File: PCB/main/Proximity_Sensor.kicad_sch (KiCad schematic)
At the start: 8 parts, among them U4 VL6180XV0NR_1

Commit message: Add sheet properties
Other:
- company: (none) -> University of Cape Town
- title: (none) -> Proximity Sensor
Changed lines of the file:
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@@
 (kicad_sch (version 20211123) (generator eeschema)
   (paper "A4")
+  (title_block
+    (title "Proximity Sensor")
+    (date "2022-03-09")
+    (rev "v1.0")
+    (company "University of Cape Town")
+    (comment 4 "Author: Kelvin Yankey")
+  )
   (junction (at 172.72 87.63) (diameter 0) (color 0 0 0 0)
   )

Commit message: Add changes
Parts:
- renumbered C5 to C7, C6 to C8, D2 to D8, D3 to D9, R7 to R11, R9 to R12, R12 to R13, U4 to U6
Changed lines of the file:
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@@
   (symbol (lib_id "Device:R") (at 85.09 46.99 0) (unit 1)
     (in_bom yes) (on_board yes) (fields_autoplaced)
-    (property "Reference" "R7" (id 0) (at 87.63 45.7199 0)
+    (property "Reference" "R11" (id 0) (at 87.63 45.7199 0)
       (effects (font (size 1.27 1.27)) (justify left))
     )
@@
   (symbol (lib_id "Device:C_Polarized") (at 151.13 53.34 270) (unit 1)
     (in_bom yes) (on_board yes) (fields_autoplaced)
-    (property "Reference" "C5" (id 0) (at 152.019 45.72 90))
+    (property "Reference" "C7" (id 0) (at 152.019 45.72 90))
     (property "Value" "100n" (id 1) (at 152.019 48.26 90))
     (property "Footprint" "Capacitor_SMD:C_01005_0402Metric" (id 2) (at 147.32 54.3052 0)
@@
   (symbol (lib_id "Device:R") (at 172.72 95.25 0) (unit 1)
     (in_bom yes) (on_board yes) (fields_autoplaced)
-    (property "Reference" "R12" (id 0) (at 175.26 93.9799 0)
+    (property "Reference" "R13" (id 0) (at 175.26 93.9799 0)
       (effects (font (size 1.27 1.27)) (justify left))
     )
@@
   (symbol (lib_id "Device:R") (at 85.09 55.88 0) (unit 1)
     (in_bom yes) (on_board yes) (fields_autoplaced)
-    (property "Reference" "R9" (id 0) (at 87.63 54.6099 0)
+    (property "Reference" "R12" (id 0) (at 87.63 54.6099 0)
       (effects (font (size 1.27 1.27)) (justify left))
     )
@@
   (symbol (lib_id "Device:C_Polarized") (at 151.13 67.31 270) (unit 1)
     (in_bom yes) (on_board yes) (fields_autoplaced)
-    (property "Reference" "C6" (id 0) (at 152.019 59.69 90))
+    (property "Reference" "C8" (id 0) (at 152.019 59.69 90))
     (property "Value" "4.7n" (id 1) (at 152.019 62.23 90))
     (property "Footprint" "" (id 2) (at 147.32 68.2752 0)
@@
   (symbol (lib_id "Diode:BZT52Bxx") (at 85.09 71.12 270) (unit 1)
     (in_bom yes) (on_board yes) (fields_autoplaced)
-    (property "Reference" "D2" (id 0) (at 87.63 69.8499 90)
+    (property "Reference" "D8" (id 0) (at 87.63 69.8499 90)
       (effects (font (size 1.27 1.27)) (justify left))
     )
@@
   (symbol (lib_id "Device:LED") (at 172.72 102.87 90) (unit 1)
     (in_bom yes) (on_board yes) (fields_autoplaced)
-    (property "Reference" "D3" (id 0) (at 176.53 103.1874 90)
+    (property "Reference" "D9" (id 0) (at 176.53 103.1874 90)
       (effects (font (size 1.27 1.27)) (justify right))
     )
@@
   (symbol (lib_id "EEE3088Components:VL6180XV0NR_1") (at 185.42 59.69 0) (unit 1)
     (in_bom yes) (on_board yes) (fields_autoplaced)
-    (property "Reference" "U4" (id 0) (at 210.82 52.07 0))
+    (property "Reference" "U6" (id 0) (at 210.82 52.07 0))
     (property "Value" "VL6180XV0NR_1" (id 1) (at 210.82 54.61 0))
     (property "Footprint" "STMicroelectronics-VL6180XV0NR_1-*" (id 2) (at 185.42 49.53 0)

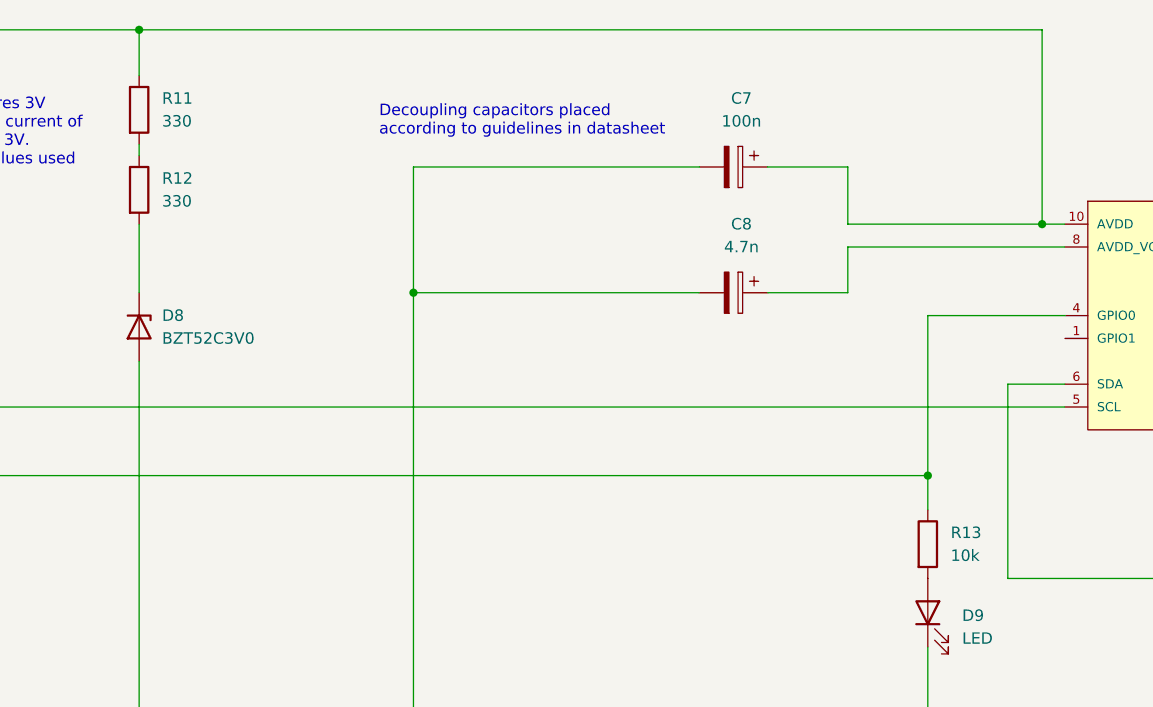
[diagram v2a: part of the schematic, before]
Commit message: Add usb sensing
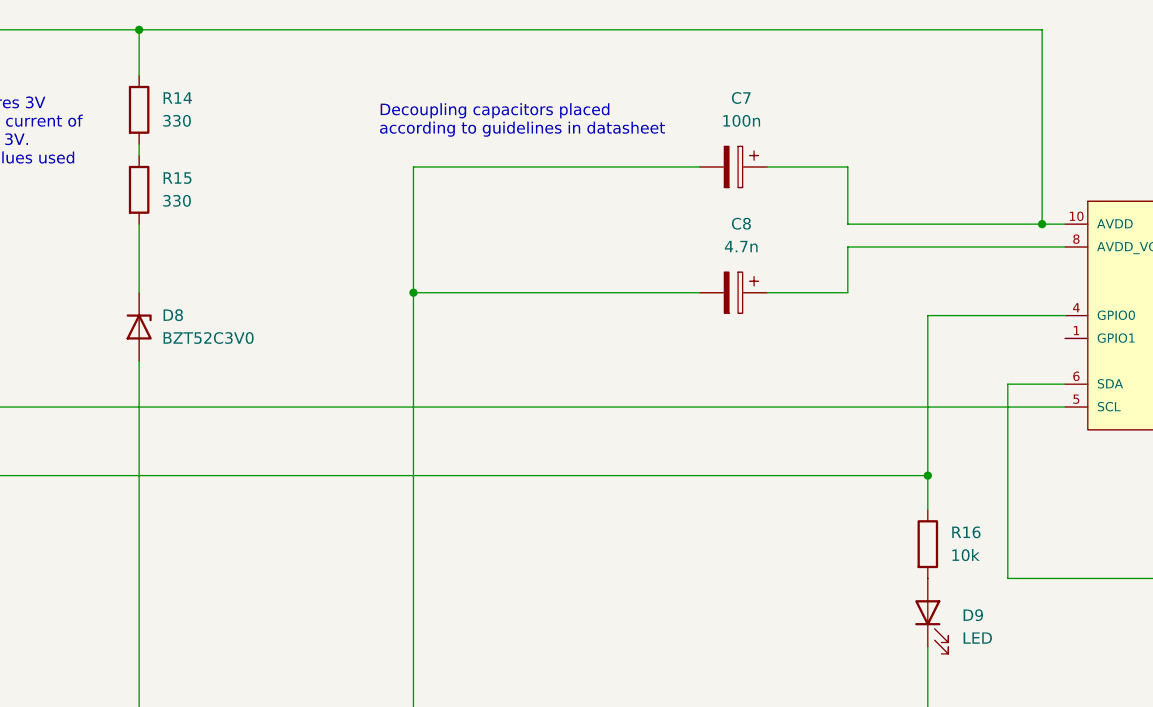
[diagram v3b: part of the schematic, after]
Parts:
- renumbered R11 to R14, R12 to R15, R13 to R16
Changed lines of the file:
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@@
   (symbol (lib_id "Device:R") (at 85.09 46.99 0) (unit 1)
     (in_bom yes) (on_board yes) (fields_autoplaced)
-    (property "Reference" "R11" (id 0) (at 87.63 45.7199 0)
+    (property "Reference" "R14" (id 0) (at 87.63 45.7199 0)
       (effects (font (size 1.27 1.27)) (justify left))
     )
@@
   (symbol (lib_id "Device:R") (at 172.72 95.25 0) (unit 1)
     (in_bom yes) (on_board yes) (fields_autoplaced)
-    (property "Reference" "R13" (id 0) (at 175.26 93.9799 0)
+    (property "Reference" "R16" (id 0) (at 175.26 93.9799 0)
       (effects (font (size 1.27 1.27)) (justify left))
     )
@@
   (symbol (lib_id "Device:R") (at 85.09 55.88 0) (unit 1)
     (in_bom yes) (on_board yes) (fields_autoplaced)
-    (property "Reference" "R12" (id 0) (at 87.63 54.6099 0)
+    (property "Reference" "R15" (id 0) (at 87.63 54.6099 0)
       (effects (font (size 1.27 1.27)) (justify left))
     )

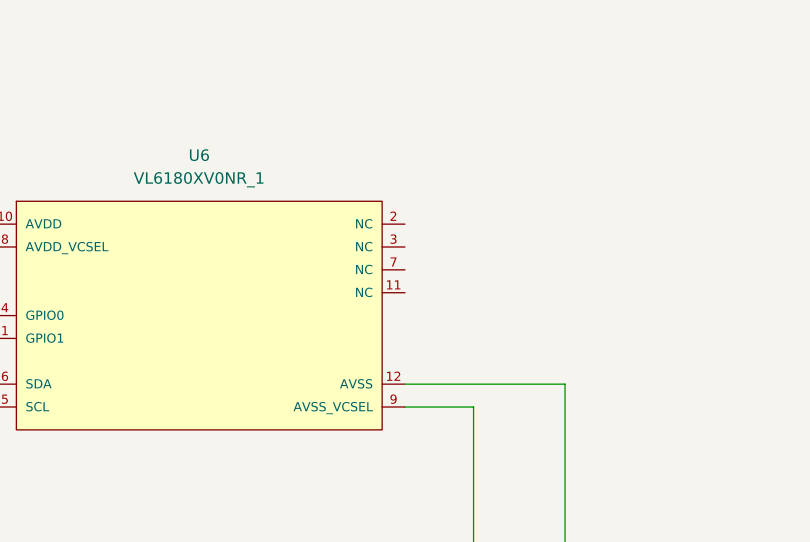
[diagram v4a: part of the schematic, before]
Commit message: Correct labels
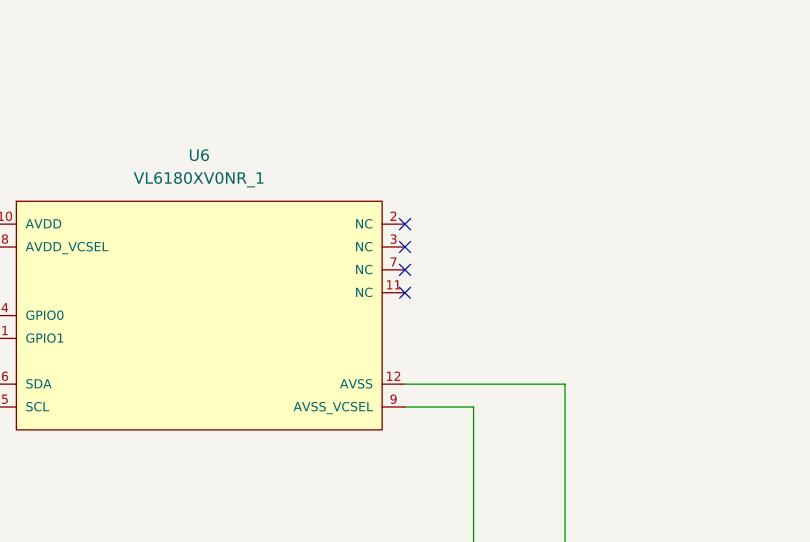
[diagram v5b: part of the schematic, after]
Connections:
- no-connect marks 0 -> 4
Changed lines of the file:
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@@
   (junction (at 185.42 59.69) (diameter 0) (color 0 0 0 0)
   )
+  (no_connect (at 233.68 62.23))
+  (no_connect (at 233.68 59.69))
+  (no_connect (at 233.68 64.77))
+  (no_connect (at 233.68 67.31))
   (wire (pts (xy 115.57 67.31) (xy 147.32 67.31))
     (stroke (width 0) (type default) (color 0 0 0 0))

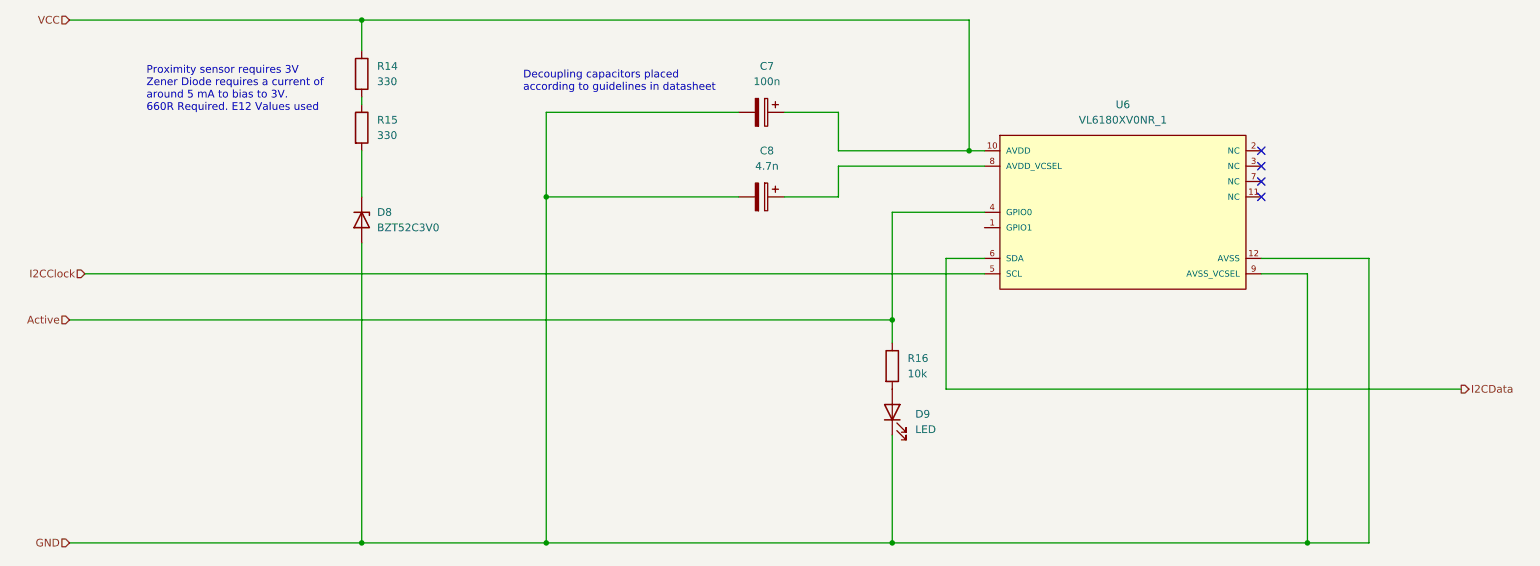
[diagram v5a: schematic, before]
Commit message: Work on reducing ERC flags
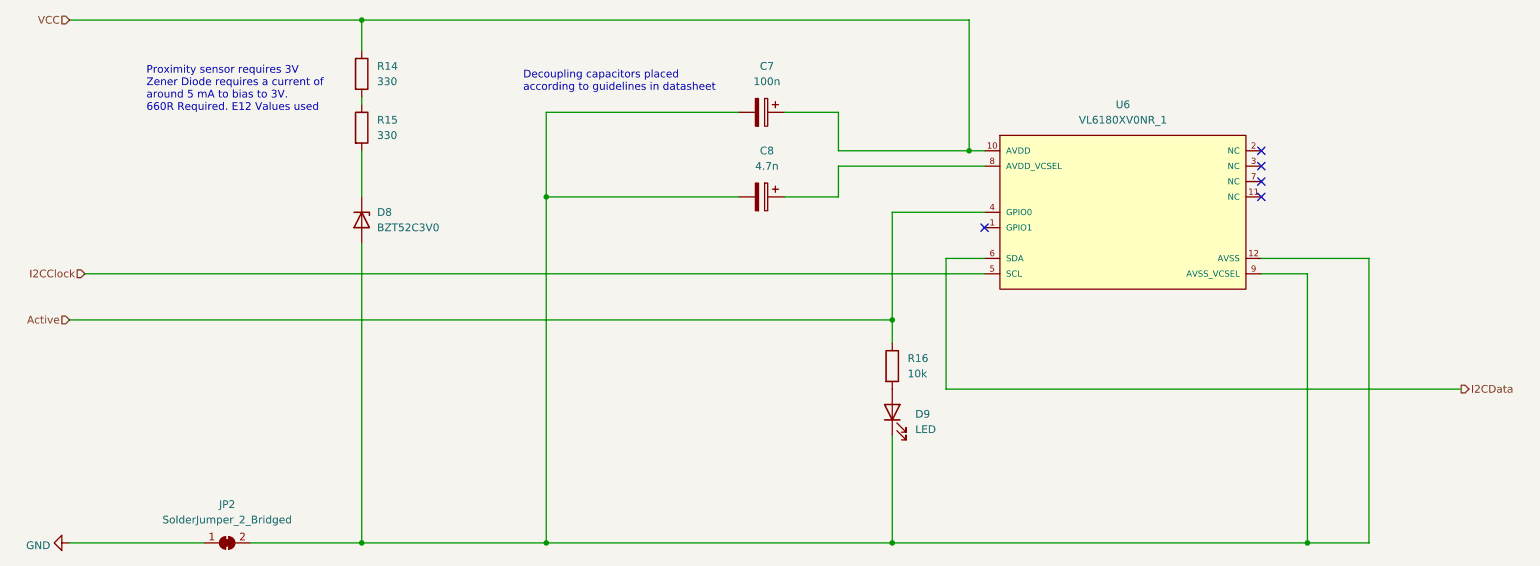
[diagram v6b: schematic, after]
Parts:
- added JP2: SolderJumper_2_Bridged, symbol Jumper:SolderJumper_2_Bridged
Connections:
- net GND: now also JP2.1 (A); no longer C7.2, C8.2, D8.2 (A), D9.1 (K), U6.12 (AVSS), U6.9 (AVSS_VCSEL)
- new net: C7.2, C8.2, D8.2 (A), D9.1 (K), JP2.2 (B), U6.12 (AVSS), U6.9 (AVSS_VCSEL)
- no-connect marks 4 -> 5
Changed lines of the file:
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@@
   (no_connect (at 233.68 64.77))
   (no_connect (at 233.68 67.31))
+  (no_connect (at 187.96 72.39))
   (wire (pts (xy 115.57 67.31) (xy 147.32 67.31))
     (stroke (width 0) (type default) (color 0 0 0 0))
@@
     (stroke (width 0) (type default) (color 0 0 0 0))
   )
-  (wire (pts (xy 36.83 124.46) (xy 85.09 124.46))
+  (wire (pts (xy 36.83 124.46) (xy 59.055 124.46))
     (stroke (width 0) (type default) (color 0 0 0 0))
   )
@@
   )
   (wire (pts (xy 172.72 87.63) (xy 172.72 91.44))
+    (stroke (width 0) (type default) (color 0 0 0 0))
+  )
+  (wire (pts (xy 66.675 124.46) (xy 85.09 124.46))
     (stroke (width 0) (type default) (color 0 0 0 0))
   )
@@
     (effects (font (size 1.27 1.27)) (justify right))
   )
-  (hierarchical_label "GND" (shape input) (at 36.83 124.46 180)
-    (effects (font (size 1.27 1.27)) (justify right))
-  )
   (hierarchical_label "I2CClock" (shape input) (at 39.37 80.01 180)
     (effects (font (size 1.27 1.27)) (justify right))
@@
     (pin "2")
   )
+  (symbol (lib_id "Jumper:SolderJumper_2_Bridged") (at 62.865 124.46 0) (unit 1)
+    (in_bom yes) (on_board yes) (fields_autoplaced)
+    (property "Reference" "JP2" (id 0) (at 62.865 118.11 0))
+    (property "Value" "SolderJumper_2_Bridged" (id 1) (at 62.865 120.65 0))
+    (property "Footprint" "" (id 2) (at 62.865 124.46 0)
+      (effects (font (size 1.27 1.27)) hide)
+    )
+    (property "Datasheet" "~" (id 3) (at 62.865 124.46 0)
+      (effects (font (size 1.27 1.27)) hide)
+    )
+    (pin "1")
+    (pin "2")
+  )
+  (symbol (lib_id "power:GND") (at 36.83 124.46 270) (unit 1)
+    (in_bom yes) (on_board yes) (fields_autoplaced)
+    (property "Reference" "#PWR0103" (id 0) (at 30.48 124.46 0)
+      (effects (font (size 1.27 1.27)) hide)
+    )
+    (property "Value" "GND" (id 1) (at 33.6551 124.8938 90)
+      (effects (font (size 1.27 1.27)) (justify right))
+    )
+    (property "Footprint" "" (id 2) (at 36.83 124.46 0)
+      (effects (font (size 1.27 1.27)) hide)
+    )
+    (property "Datasheet" "" (id 3) (at 36.83 124.46 0)
+      (effects (font (size 1.27 1.27)) hide)
+    )
+    (pin "1")
+  )
   (symbol (lib_id "Device:R") (at 172.72 95.25 0) (unit 1)

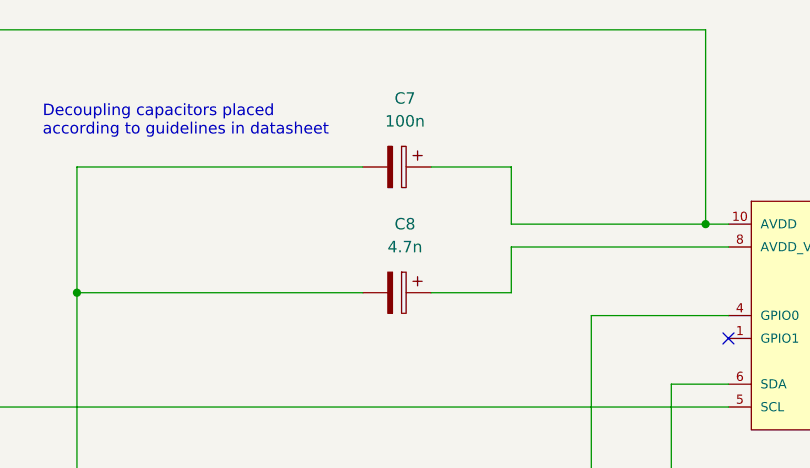
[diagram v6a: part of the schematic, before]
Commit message: Add footprints
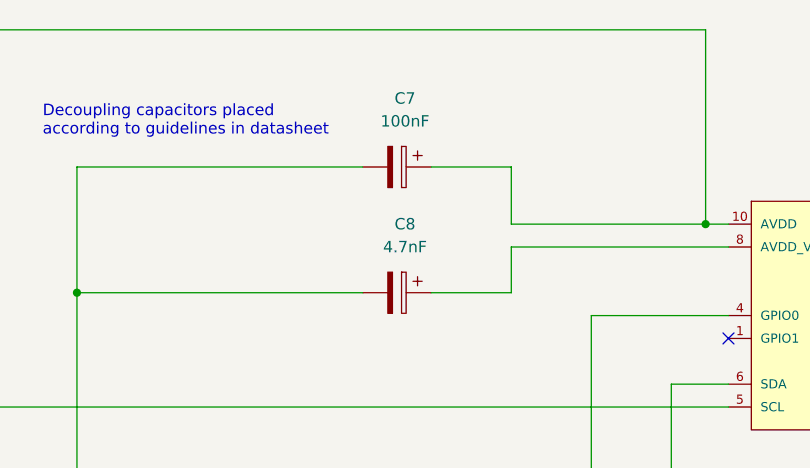
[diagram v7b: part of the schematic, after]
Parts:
- C7: value 100n -> 100nF; footprint Capacitor_SMD:C_01005_0402Metric -> Capacitor_SMD:C_0402_1005Metric
- C8: value 4.7n -> 4.7nF; footprint (none) -> Capacitor_SMD:C_0402_1005Metric
- D9: footprint (none) -> LED_SMD:LED_0603_1608Metric
- JP2: footprint (none) -> Jumper:SolderJumper-2_P1.3mm_Bridged2Bar_Pad1.0x1.5mm
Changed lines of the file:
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@@
     (in_bom yes) (on_board yes) (fields_autoplaced)
     (property "Reference" "C7" (id 0) (at 152.019 45.72 90))
-    (property "Value" "100n" (id 1) (at 152.019 48.26 90))
-    (property "Footprint" "Capacitor_SMD:C_01005_0402Metric" (id 2) (at 147.32 54.3052 0)
+    (property "Value" "100nF" (id 1) (at 152.019 48.26 90))
+    (property "Footprint" "Capacitor_SMD:C_0402_1005Metric" (id 2) (at 147.32 54.3052 0)
       (effects (font (size 1.27 1.27)) hide)
     )
@@
     (property "Reference" "JP2" (id 0) (at 62.865 118.11 0))
     (property "Value" "SolderJumper_2_Bridged" (id 1) (at 62.865 120.65 0))
-    (property "Footprint" "" (id 2) (at 62.865 124.46 0)
+    (property "Footprint" "Jumper:SolderJumper-2_P1.3mm_Bridged2Bar_Pad1.0x1.5mm" (id 2) (at 62.865 124.46 0)
       (effects (font (size 1.27 1.27)) hide)
     )
@@
     (in_bom yes) (on_board yes) (fields_autoplaced)
     (property "Reference" "C8" (id 0) (at 152.019 59.69 90))
-    (property "Value" "4.7n" (id 1) (at 152.019 62.23 90))
-    (property "Footprint" "" (id 2) (at 147.32 68.2752 0)
+    (property "Value" "4.7nF" (id 1) (at 152.019 62.23 90))
+    (property "Footprint" "Capacitor_SMD:C_0402_1005Metric" (id 2) (at 147.32 68.2752 0)
       (effects (font (size 1.27 1.27)) hide)
     )
@@
       (effects (font (size 1.27 1.27)) (justify right))
     )
-    (property "Footprint" "" (id 2) (at 172.72 102.87 0)
+    (property "Footprint" "LED_SMD:LED_0603_1608Metric" (id 2) (at 172.72 102.87 0)
       (effects (font (size 1.27 1.27)) hide)
     )
